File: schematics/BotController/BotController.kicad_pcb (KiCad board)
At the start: 2 copper layers, 54 parts, among them IC1 ATMEGA644A-P, P1 2x Serial, P10 Stepper Upperarm, P11 Stepper Shoulder, P12 POWER_IN, P13 PowerEnableIn, P17 PowerEnableOut, P2 Herkulex Servo, P28 Power Stepper, P3 Encoder Socket 0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

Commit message: Neuer Oberarm mit horizontalem Riemenspanner
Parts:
- P10: value Stepper Upperarm -> Stepper Shoulder
- P11: value Stepper Shoulder -> Stepper Hip
- P8: value Stepper Ellbow -> Stepper Forearm
- P9: value Stepper Forearm -> Stepper Upperarm
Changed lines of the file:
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@@
       (effects (font (size 1 1) (thickness 0.15)))
     )
-    (fp_text value "Stepper Ellbow" (at 3.81 4.5 180) (layer F.Fab)
+    (fp_text value "Stepper Forearm" (at 3.81 4.5 180) (layer F.Fab)
       (effects (font (size 1 1) (thickness 0.15)))
     )
@@
       (effects (font (size 1 1) (thickness 0.15)))
     )
-    (fp_text value "Stepper Forearm" (at 3.81 4.5 180) (layer F.Fab)
+    (fp_text value "Stepper Upperarm" (at 3.81 4.5 180) (layer F.Fab)
       (effects (font (size 1 1) (thickness 0.15)))
     )
@@
       (effects (font (size 1 1) (thickness 0.15)))
     )
-    (fp_text value "Stepper Upperarm" (at 3.81 4.5 180) (layer F.Fab)
+    (fp_text value "Stepper Shoulder" (at 3.81 4.5 180) (layer F.Fab)
       (effects (font (size 1 1) (thickness 0.15)))
     )
@@
       (effects (font (size 1 1) (thickness 0.15)))
     )
-    (fp_text value "Stepper Shoulder" (at 3.81 4.5 180) (layer F.Fab)
+    (fp_text value "Stepper Hip" (at 3.81 4.5 180) (layer F.Fab)
       (effects (font (size 1 1) (thickness 0.15)))
     )
@@
   (segment (start 121.92 119.38) (end 121.92 119.38) (width 0.25) (layer B.Cu) (net 5) (status 30))
   (segment (start 77.47 149.78) (end 77.47 157.48) (width 0.25) (layer B.Cu) (net 6))
-  (segment (start 77.47 157.48) (end 81.28 157.48) (width 0.25) (layer B.Cu) (net 6) (status 800000))
+  (segment (start 77.47 157.48) (end 81.28 157.48) (width 0.25) (layer B.Cu) (net 6))
   (segment (start 66.04 147.32) (end 66.04 148.59) (width 0.25) (layer B.Cu) (net 6))
   (segment (start 66.04 149.86) (end 68.58 149.86) (width 0.25) (layer B.Cu) (net 6))

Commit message: no message
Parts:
- added P14: Power Stepper 2, Connect:bornier2, F.Cu at (129.5, 71.1)
- added P15: Power Stepper 3, Connect:bornier2, F.Cu at (129.5, 63.5)
- added P16: Power Stepper 4, Connect:bornier2, F.Cu at (129.5, 55.9)
- added P18: Power Stepper 5, Connect:bornier2, F.Cu at (129.5, 48.3)
- P28: value Power Stepper -> Power Stepper 1
- moved P7 16.1 mm to (132.1, 38.1), turned to 180 degrees
- moved P28 5.68 mm to (129.5, 78.7), turned to 0 degrees
- moved U2 2.54 mm to (114.3, 43.2)
- moved C6 1.27 mm to (119.4, 58.4)
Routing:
- net GNDPWR: track 585.5 -> 621.7 mm
- net /VDD_uC: track 15.2 -> 33.0 mm
- net /VDD_Servo: track 53.3 -> 43.2 mm
- net Net-(C11-Pad1): track 96.5 -> 94.0 mm
- net Net-(P14-Pad1): track 66.0 -> 64.0 mm

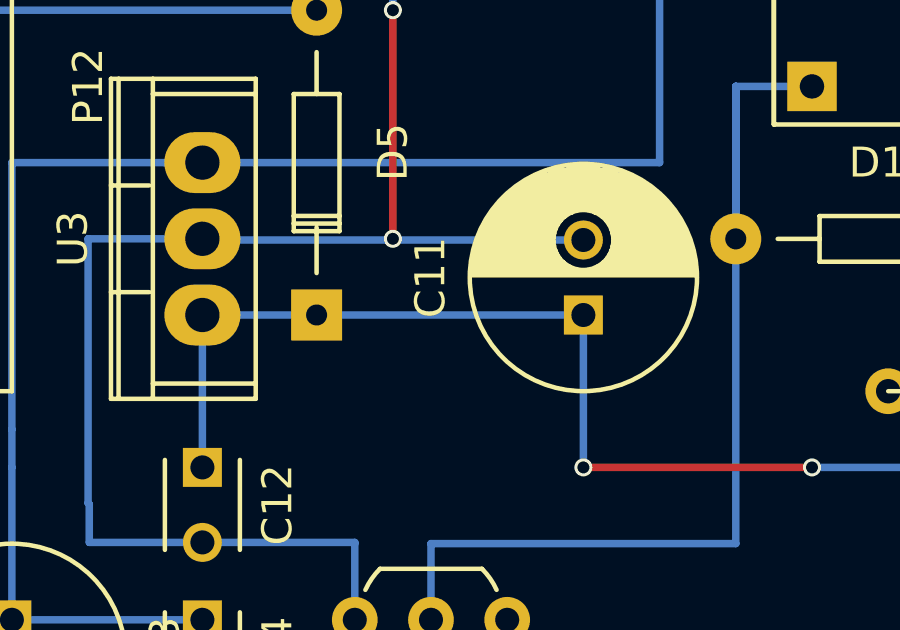
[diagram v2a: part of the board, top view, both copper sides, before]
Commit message: einzelne Motoren Regelung eingestellt
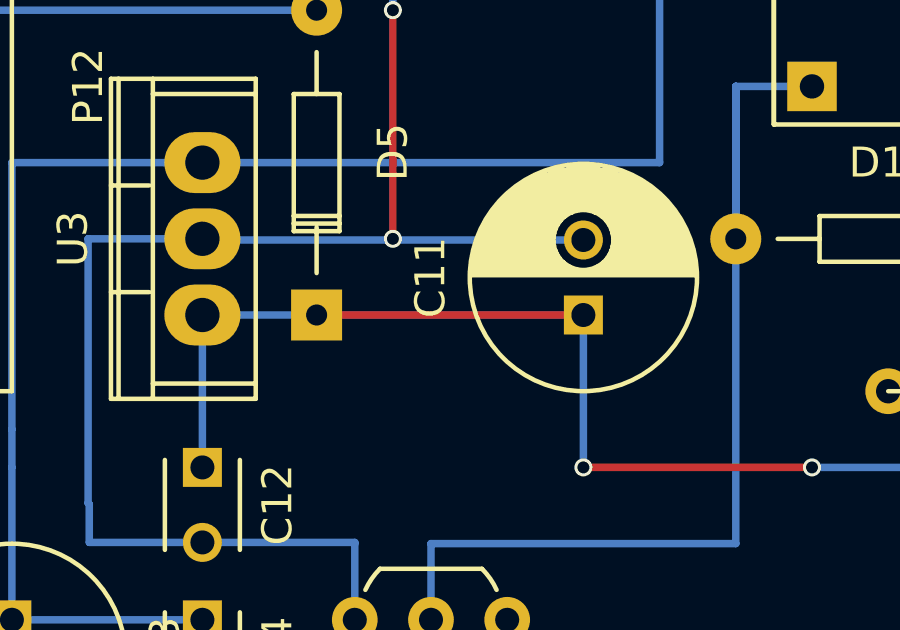
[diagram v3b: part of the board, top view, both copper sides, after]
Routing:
- net Net-(C11-Pad1): track 94.0 -> 102.9 mm
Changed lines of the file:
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@@
   (general
     (links 137)
-    (no_connects 5)
+    (no_connects 4)
     (area 34.33 30.154999 148.55 191.73)
     (thickness 1.6)
     (drawings 4)
-    (tracks 443)
+    (tracks 445)
     (zones 0)
     (modules 58)
@@
   (segment (start 106.68 124.46) (end 116.84 124.46) (width 0.25) (layer B.Cu) (net 5) (status 10))
   (segment (start 121.92 119.38) (end 121.92 119.38) (width 0.25) (layer B.Cu) (net 5) (status 30))
-  (segment (start 114.3 43.18) (end 114.3 50.8) (width 0.25) (layer B.Cu) (net 6) (status 400000))
-  (segment (start 114.3 50.8) (end 116.88 50.8) (width 0.25) (layer B.Cu) (net 6) (status 800000))
+  (segment (start 114.3 43.18) (end 114.3 50.8) (width 0.25) (layer B.Cu) (net 6))
+  (segment (start 114.3 50.8) (end 116.88 50.8) (width 0.25) (layer B.Cu) (net 6))
   (segment (start 132.08 63.5) (end 132.08 71.12) (width 0.25) (layer B.Cu) (net 6))
   (segment (start 132.08 71.12) (end 132.08 78.74) (width 0.25) (layer B.Cu) (net 6))
@@
   (segment (start 99.06 58.42) (end 99.06 66.04202) (width 0.25) (layer B.Cu) (net 35) (status 10))
   (segment (start 99.06 66.04202) (end 99.05948 66.04254) (width 0.25) (layer B.Cu) (net 35) (status 30))
-  (segment (start 111.76 48.26) (end 111.76 43.18) (width 0.25) (layer B.Cu) (net 36) (status C00000))
+  (segment (start 67.30746 66.03948) (end 76.19948 66.03948) (width 0.25) (layer F.Cu) (net 36) (status C00000))
+  (segment (start 76.19948 66.03948) (end 76.2 66.04) (width 0.25) (layer F.Cu) (net 36) (status C00000))
+  (segment (start 111.76 48.26) (end 111.76 43.18) (width 0.25) (layer B.Cu) (net 36))
   (segment (start 76.2 66.04) (end 76.2 71.12) (width 0.25) (layer B.Cu) (net 36))
   (segment (start 83.82 71.12) (end 96.52 71.12) (width 0.25) (layer B.Cu) (net 36))
@@
   (segment (start 50.8 119.38) (end 50.8 177.8) (width 0.25) (layer B.Cu) (net 41))
   (segment (start 119.38 43.18) (end 119.38 40.64) (width 0.25) (layer B.Cu) (net 42))
-  (segment (start 116.84 43.18) (end 119.38 43.18) (width 0.25) (layer B.Cu) (net 42) (status 400000))
-  (segment (start 119.38 43.18) (end 119.38 50.8) (width 0.25) (layer B.Cu) (net 42) (status 800000))
+  (segment (start 116.84 43.18) (end 119.38 43.18) (width 0.25) (layer B.Cu) (net 42))
+  (segment (start 119.38 43.18) (end 119.38 50.8) (width 0.25) (layer B.Cu) (net 42))
   (segment (start 119.38 58.42) (end 119.38 50.8) (width 0.25) (layer B.Cu) (net 42))
   (segment (start 129.54 40.64) (end 127 40.64) (width 0.25) (layer B.Cu) (net 42))
@@
   (via (at 121.92 35.56) (size 0.6) (drill 0.4) (layers F.Cu B.Cu) (net 54))
   (segment (start 121.92 35.56) (end 121.92 35.56) (width 0.25) (layer B.Cu) (net 54))
-  (segment (start 127 48.26) (end 121.92 48.26) (width 0.25) (layer B.Cu) (net 54) (status 400000))
+  (segment (start 127 48.26) (end 121.92 48.26) (width 0.25) (layer B.Cu) (net 54))
   (segment (start 127 62.86359) (end 126.681795 63.181795) (width 0.25) (layer B.Cu) (net 54))
   (segment (start 106.68 35.56) (end 121.92 35.56) (width 0.25) (layer B.Cu) (net 54))

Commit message: Power PCB works!
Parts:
- added P19: ODroid Power, Connect:bornier2, F.Cu at (6.35, 116.8)
- C12, P12: moved to B.Cu
- Q1, Q2: value Q_NPN_BCE -> BC237; footprint TO_SOT_Packages_THT:TO-92_Inline_Wide -> TO_SOT_Packages_THT:TO-92_Molded_Wide
- moved P28 177.2 mm to (-19.1, 175.3), turned to 270 degrees
- moved P7 176.6 mm to (17.8, 172.7), turned to 0 degrees
- moved P14 175.3 mm to (-11.4, 175.3), turned to 270 degrees
- moved P15 174.0 mm to (-3.81, 175.3), turned to 270 degrees
- moved P18 173.4 mm to (11.4, 175.3), turned to 270 degrees
- moved P16 173.4 mm to (3.81, 175.3), turned to 270 degrees
- moved Q2 162.4 mm to (-19.1, 165.1), turned to 0 degrees
- moved C6 161.8 mm to (0.00, 167.6), turned to 90 degrees
- moved C3 159.9 mm to (7.62, 165.1), turned to 90 degrees
- moved U2 153.5 mm to (17.8, 162.6), turned to 270 degrees
- moved R5 150.9 mm to (5.08, 160.0), turned to 0 degrees
- moved D10 148.0 mm to (-5.08, 160.0), turned to 90 degrees
- moved R10 147.6 mm to (-21.6, 160.0), turned to 90 degrees
- moved C4 140.6 mm to (-16.5, 149.9), turned to 270 degrees
- moved REL2 138.6 mm to (0.00, 149.9), turned to 270 degrees
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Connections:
- P12 pad 3: (no net) -> /5V
- Q1 pad 1: Net-(Q1-Pad1) -> Net-(D1-Pad2)
- Q1 pad 2: Net-(D1-Pad2) -> Net-(Q1-Pad2)
- Q2 pad 1: Net-(Q2-Pad1) -> Net-(D10-Pad2)
- Q2 pad 2: Net-(D10-Pad2) -> Net-(Q2-Pad2)
- R10 pad 1: Net-(Q2-Pad1) -> Net-(Q2-Pad2)
- R8 pad 1: Net-(Q1-Pad1) -> Net-(Q1-Pad2)
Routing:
- net Net-(C13-Pad1): track 71.1 -> 102.9 mm
- net Net-(C11-Pad1): track 102.9 -> 134.6 mm
- net /5V: track 0.00 -> 19.0 mm
- net Net-(D1-Pad2): track 35.6 -> 21.6 mm
- net Net-(Q2-Pad1): track 12.7 -> 0.00 mm
- net Net-(Q2-Pad2): track 0.00 -> 12.7 mm
- net GNDPWR: track 621.7 -> 613.9 mm, vias 10 -> 8
- net /PowerOnStepper: track 5.08 -> 12.7 mm
- net Net-(C4-Pad2): track 25.4 -> 31.8 mm
- net /12V: track 14.0 -> 7.62 mm
- net /PowerOnServo: track 5.08 -> 0.00 mm
- net (no net): track 0.00 -> 4.01 mm
- net Net-(F1-Pad2): track 33.0 -> 30.5 mm
- net Net-(Q1-Pad1): track 2.54 -> 0.00 mm
- net /VDD_uC: track 33.0 -> 30.5 mm
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
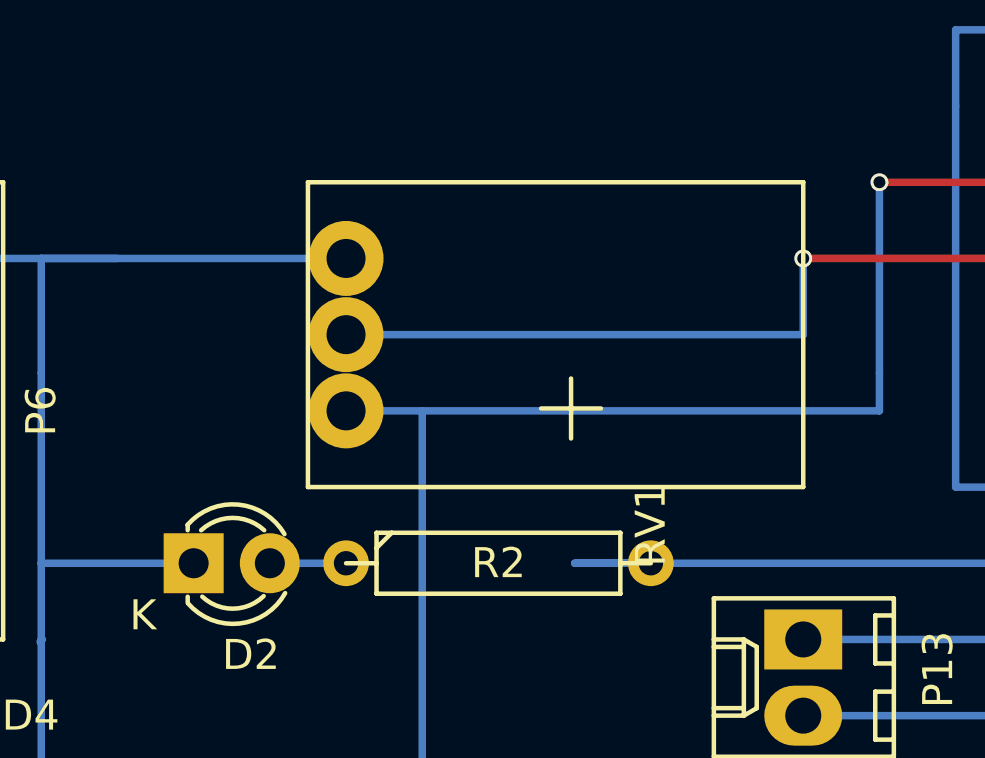
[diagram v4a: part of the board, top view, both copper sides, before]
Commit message: added power supply to the housing
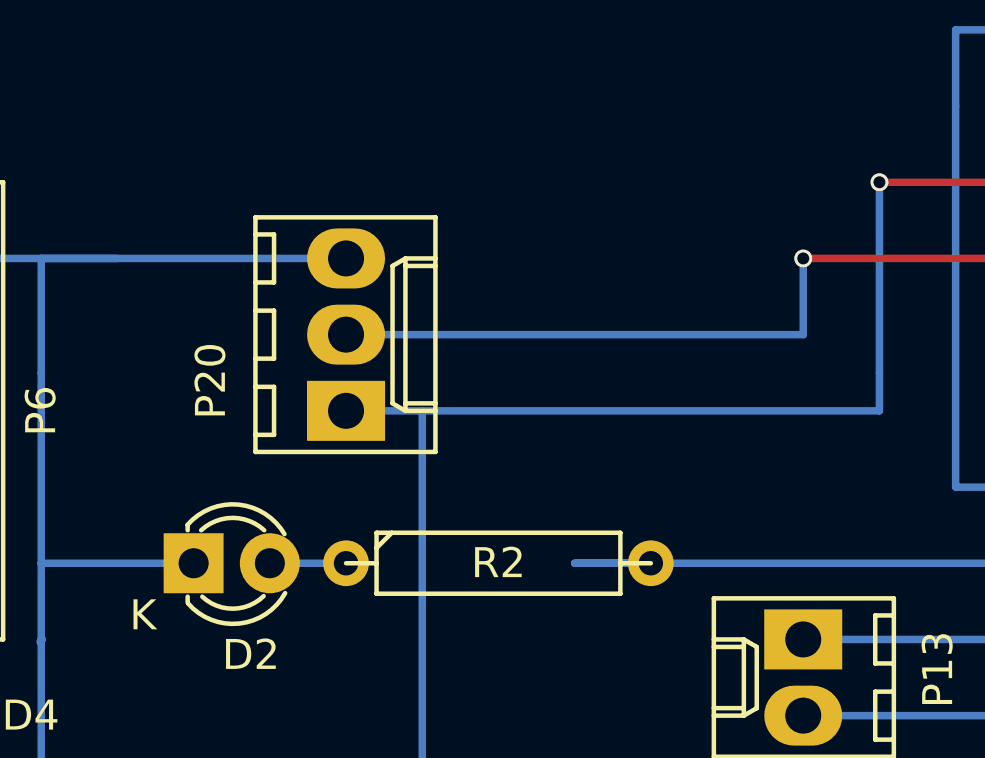
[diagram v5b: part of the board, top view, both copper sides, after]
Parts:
- removed RV1: 10K, BotController:Potentiometer_Trimmer-ALPS-horizontal
- added P20: POTI 10K, Connectors_Molex:Molex_KK_6410-03, F.Cu at (68.6, 114.3)
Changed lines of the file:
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@@
     )
-  )
-  (module BotController:Potentiometer_Trimmer-ALPS-horizontal (layer F.Cu)
-    (at 68.58 109.22 270)
-    (descr "Potentiometer, Trimmer, ALPS ")
-    (tags "Potentiometer, Trimmer, Piher, PT15, Type V12.5, horizontal, Rev A, 02 Aug 2010,")
-    (fp_text reference RV1 (at 8.89 -10.16 270) (layer F.SilkS)
-      (effects (font (size 1 1) (thickness 0.15)))
-    )
-    (fp_text value 10K (at 3.73126 3.92938 270) (layer F.Fab)
-      (effects (font (size 1 1) (thickness 0.15)))
-    )
-    (fp_line (start -2.54 1.27) (end 7.62 1.27) (layer F.SilkS) (width 0.15))
-    (fp_line (start -2.54 -15.24) (end 7.62 -15.24) (layer F.SilkS) (width 0.15))
-    (fp_line (start 7.62 1.27) (end 7.62 -15.24) (layer F.SilkS) (width 0.15))
-    (fp_line (start -2.54 -15.24) (end -2.54 1.27) (layer F.SilkS) (width 0.15))
-    (fp_line (start 5.00126 -8.50138) (end 5.00126 -6.49986) (layer F.SilkS) (width 0.15))
-    (fp_line (start 4.0005 -7.50062) (end 6.00202 -7.50062) (layer F.SilkS) (width 0.15))
-    (pad 2 thru_hole circle (at 2.54 0 270) (size 2.49936 2.49936) (drill 1.30048) (layers *.Cu *.Mask F.SilkS)
-      (net 28 "Net-(IC1-Pad40)"))
-    (pad 3 thru_hole circle (at 5.08 0 270) (size 2.49936 2.49936) (drill 1.30048) (layers *.Cu *.Mask F.SilkS)
-      (net 2 /+5V))
-    (pad 1 thru_hole circle (at 0 0 270) (size 2.49936 2.49936) (drill 1.30048) (layers *.Cu *.Mask F.SilkS)
-      (net 6 GNDPWR))
   )
   (module Connect:bornier2 (layer F.Cu)
@@
       (rotate (xyz 0 0 -90))
     )
+  )
+  (module Connectors_Molex:Molex_KK_6410-03 (layer F.Cu)
+    (at 68.58 114.3 90)
+    (descr "Connector Headers with Friction Lock, 22-27-2031, http://www.molex.com/pdm_docs/sd/022272021_sd.pdf")
+    (tags "connector molex kk_6410 22-27-2031")
+    (fp_text reference P20 (at 1 -4.5 90) (layer F.SilkS)
+      (effects (font (size 1 1) (thickness 0.15)))
+    )
+    (fp_text value "POTI 10K" (at 2.54 4.5 90) (layer F.Fab)
+      (effects (font (size 1 1) (thickness 0.15)))
+    )
+    (fp_line (start -1.37 -3.02) (end -1.37 2.98) (layer F.SilkS) (width 0.15))
+    (fp_line (start -1.37 2.98) (end 6.45 2.98) (layer F.SilkS) (width 0.15))
+    (fp_line (start 6.45 2.98) (end 6.45 -3.02) (layer F.SilkS) (width 0.15))
+    (fp_line (start 6.45 -3.02) (end -1.37 -3.02) (layer F.SilkS) (width 0.15))
+    (fp_line (start 0 2.98) (end 0 1.98) (layer F.SilkS) (width 0.15))
+    (fp_line (start 0 1.98) (end 5.08 1.98) (layer F.SilkS) (width 0.15))
+    (fp_line (start 5.08 1.98) (end 5.08 2.98) (layer F.SilkS) (width 0.15))
+    (fp_line (start 0 1.98) (end 0.25 1.55) (layer F.SilkS) (width 0.15))
+    (fp_line (start 0.25 1.55) (end 4.83 1.55) (layer F.SilkS) (width 0.15))
+    (fp_line (start 4.83 1.55) (end 5.08 1.98) (layer F.SilkS) (width 0.15))
+    (fp_line (start 0.25 2.98) (end 0.25 1.98) (layer F.SilkS) (width 0.15))
+    (fp_line (start 4.83 2.98) (end 4.83 1.98) (layer F.SilkS) (width 0.15))
+    (fp_line (start -0.8 -3.02) (end -0.8 -2.4) (layer F.SilkS) (width 0.15))
+    (fp_line (start -0.8 -2.4) (end 0.8 -2.4) (layer F.SilkS) (width 0.15))
+    (fp_line (start 0.8 -2.4) (end 0.8 -3.02) (layer F.SilkS) (width 0.15))
+    (fp_line (start 1.74 -3.02) (end 1.74 -2.4) (layer F.SilkS) (width 0.15))
+    (fp_line (start 1.74 -2.4) (end 3.34 -2.4) (layer F.SilkS) (width 0.15))
+    (fp_line (start 3.34 -2.4) (end 3.34 -3.02) (layer F.SilkS) (width 0.15))
+    (fp_line (start 4.28 -3.02) (end 4.28 -2.4) (layer F.SilkS) (width 0.15))
+    (fp_line (start 4.28 -2.4) (end 5.88 -2.4) (layer F.SilkS) (width 0.15))
+    (fp_line (start 5.88 -2.4) (end 5.88 -3.02) (layer F.SilkS) (width 0.15))
+    (fp_line (start -1.9 3.5) (end -1.9 -3.55) (layer F.CrtYd) (width 0.05))
+    (fp_line (start -1.9 -3.55) (end 7 -3.55) (layer F.CrtYd) (width 0.05))
+    (fp_line (start 7 -3.55) (end 7 3.5) (layer F.CrtYd) (width 0.05))
+    (fp_line (start 7 3.5) (end -1.9 3.5) (layer F.CrtYd) (width 0.05))
+    (pad 1 thru_hole rect (at 0 0 90) (size 2 2.6) (drill 1.2) (layers *.Cu *.Mask F.SilkS)
+      (net 2 /+5V))
+    (pad 2 thru_hole oval (at 2.54 0 90) (size 2 2.6) (drill 1.2) (layers *.Cu *.Mask F.SilkS)
+      (net 28 "Net-(IC1-Pad40)"))
+    (pad 3 thru_hole oval (at 5.08 0 90) (size 2 2.6) (drill 1.2) (layers *.Cu *.Mask F.SilkS)
+      (net 6 GNDPWR))
   )
   (target plus (at 19.05 96.52) (size 5) (width 0.1) (layer Edge.Cuts))
@@
   (segment (start 106.68 124.46) (end 116.84 124.46) (width 0.25) (layer B.Cu) (net 5) (status 10))
   (segment (start 121.92 119.38) (end 121.92 119.38) (width 0.25) (layer B.Cu) (net 5) (status 30))
-  (segment (start 17.78 162.56) (end 20.32 162.56) (width 0.25) (layer B.Cu) (net 6) (status 400000))
-  (segment (start 12.7 119.38) (end 6.35 119.38) (width 0.25) (layer B.Cu) (net 6) (status 800000))
+  (segment (start 17.78 162.56) (end 20.32 162.56) (width 0.25) (layer B.Cu) (net 6))
+  (segment (start 12.7 119.38) (end 6.35 119.38) (width 0.25) (layer B.Cu) (net 6))
   (segment (start 12.7 154.94) (end 12.7 119.38) (width 0.25) (layer B.Cu) (net 6))
   (segment (start 20.32 154.94) (end 12.7 154.94) (width 0.25) (layer B.Cu) (net 6))
   (segment (start 20.32 162.56) (end 20.32 154.94) (width 0.25) (layer B.Cu) (net 6))
-  (segment (start 0 119.38) (end 0 121.88) (width 0.25) (layer B.Cu) (net 6) (status 800000))
-  (segment (start 0 121.88) (end -0.04 121.92) (width 0.25) (layer B.Cu) (net 6) (status C00000))
+  (segment (start 0 119.38) (end 0 121.88) (width 0.25) (layer B.Cu) (net 6))
+  (segment (start 0 121.88) (end -0.04 121.92) (width 0.25) (layer B.Cu) (net 6))
   (segment (start -7.62 104.14) (end -7.62 119.38) (width 0.25) (layer B.Cu) (net 6))
   (segment (start -7.62 119.38) (end 0 119.38) (width 0.25) (layer B.Cu) (net 6))
